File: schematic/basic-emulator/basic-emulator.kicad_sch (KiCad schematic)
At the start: 10 parts

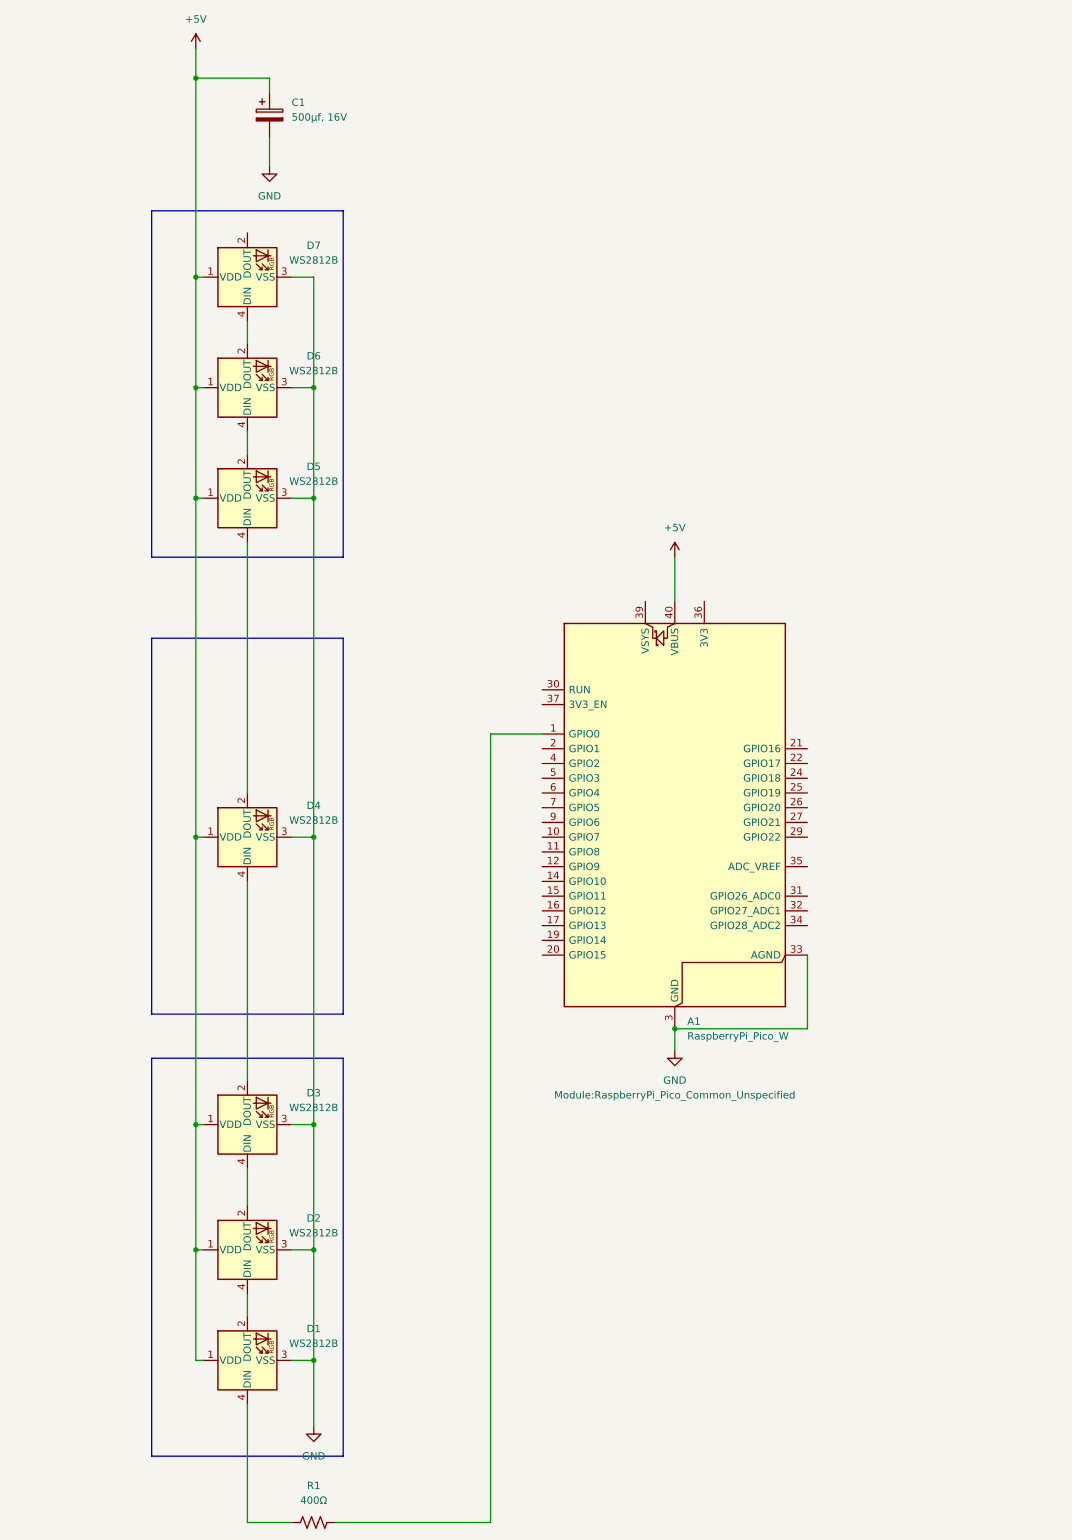
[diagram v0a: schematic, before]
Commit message: Add websockets support for colors + extra packets
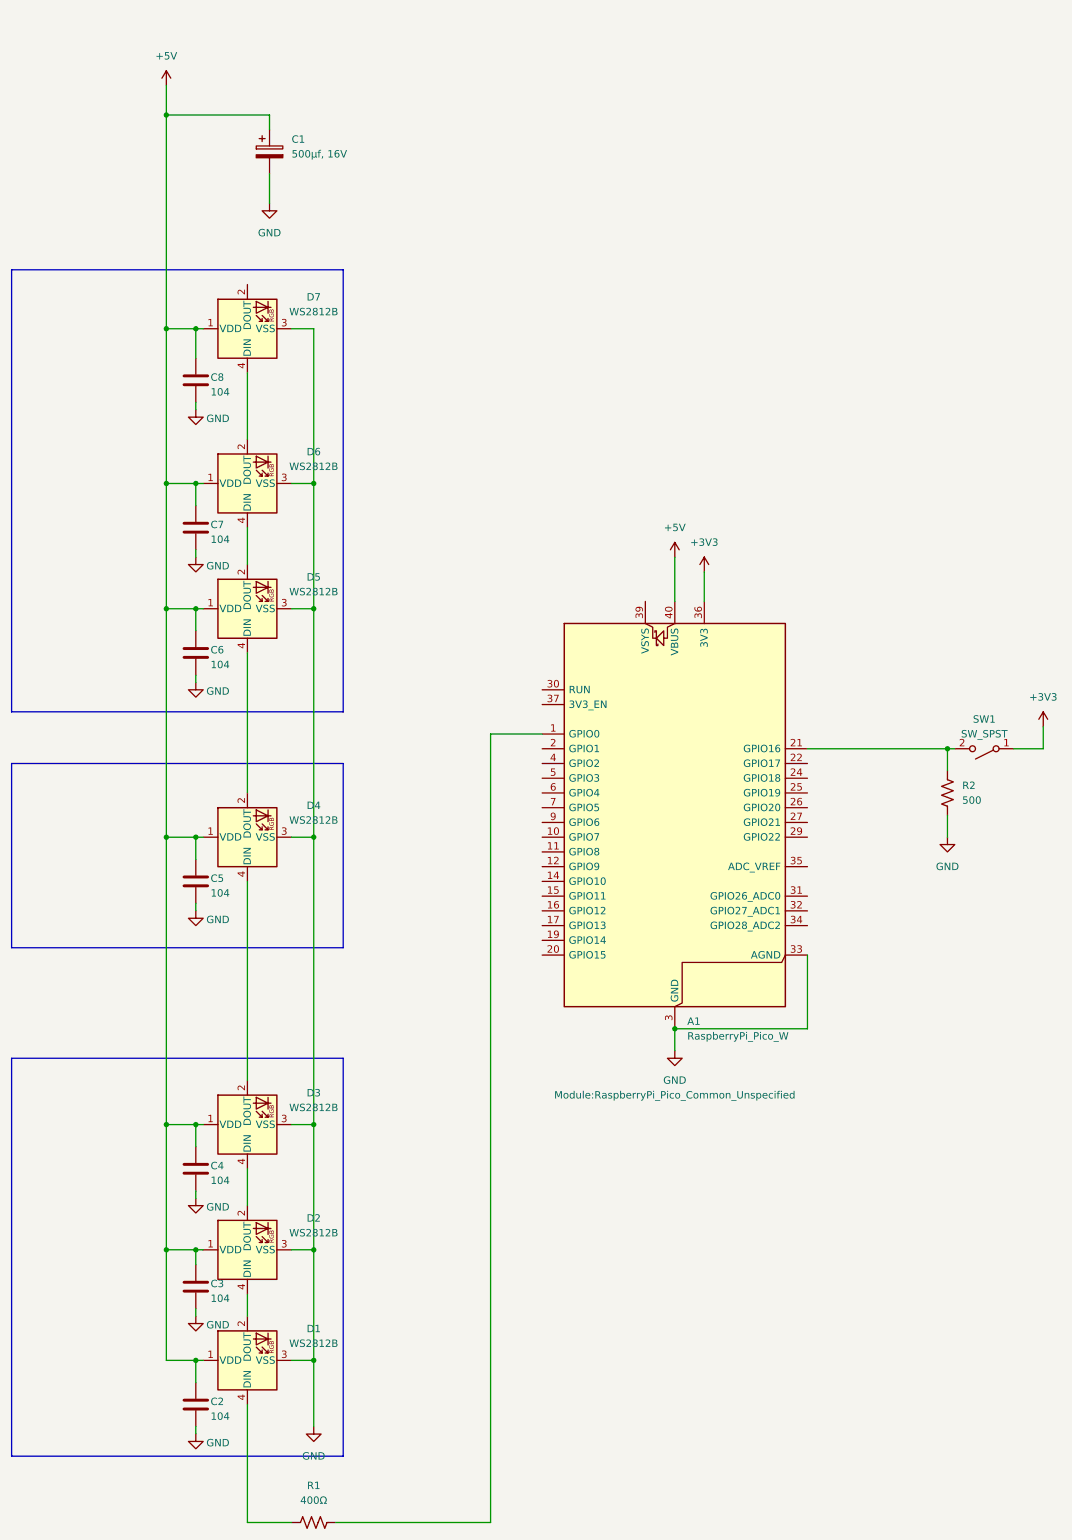
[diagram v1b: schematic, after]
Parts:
- added C2, C3, C4, C5, C6, C7, C8: 104, Capacitor_SMD:C_1206_3216Metric_Pad1.33x1.80mm_HandSolder, symbol Device:C
- added R2: 500, Resistor_SMD:R_1206_3216Metric_Pad1.30x1.75mm_HandSolder, symbol Device:R_US
- added SW1: SW_SPST, symbol Switch:SW_SPST
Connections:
- net +5V: now also C2.1, C3.1, C4.1, C5.1, C6.1, C7.1, C8.1
- net GND: now also C2.2, C3.2, C4.2, C5.2, C6.2, C7.2, C8.2, R2.2
- net at A1.21 (GPIO16): now also R2.1, SW1.2 (B)
- net +3V3: now reaches A1.36 (3V3)
- net +3V3: now also SW1.1 (A)
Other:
- moved on the sheet: C1, D5, D6, D7
